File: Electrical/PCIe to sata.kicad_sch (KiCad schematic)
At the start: 106 parts, among them J10 87427-0442, J13 SATA-A-PL-SMT-K, J14 SATA-A-PL-SMT-K, J19 SATA-A-PL-SMT-K, J20 SATA-A-PL-SMT-K, J21 SATA-A-PL-SMT-K, J22 SATA-A-PL-SMT-K, J7 87427-0442, J8 87427-0442, J9 87427-0442, U11 W25Q128JVSIQ, U8 ASM1166, Y2 25MHz

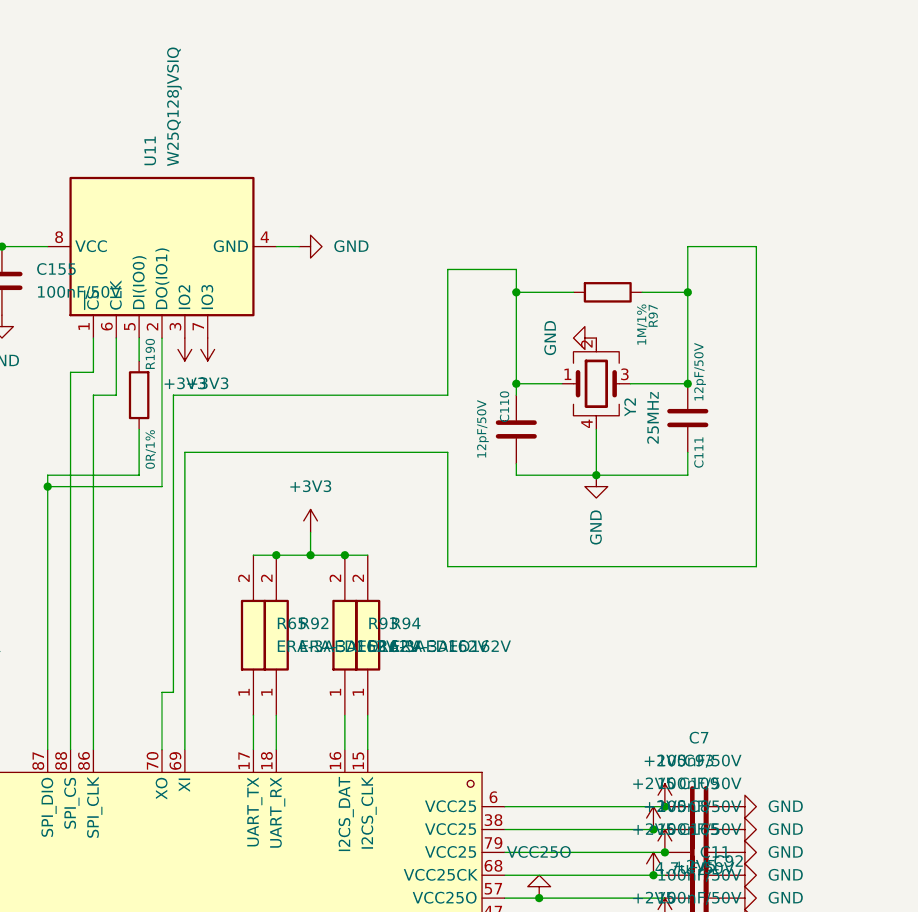
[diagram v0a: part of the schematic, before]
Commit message: add some fixes from initial prototype and fix 1v0 regulator
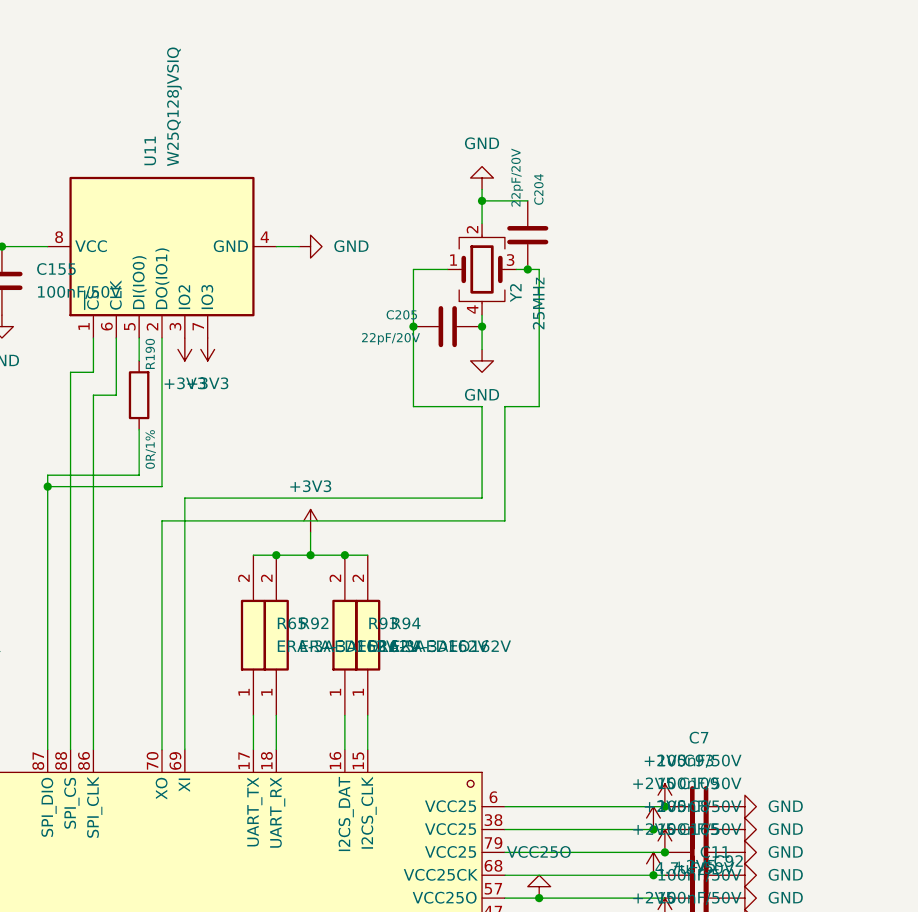
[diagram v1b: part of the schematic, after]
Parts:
- removed C110, C111: 12pF/50V, Capacitor_SMD:C_0402_1005Metric, symbol Device:C
- removed R97: 1M/1%, Resistor_SMD:R_0402_1005Metric, symbol Device:R
- added C204, C205: 22pF/20V, Capacitor_SMD:C_0402_1005Metric, symbol Device:C
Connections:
- net GND: now also C204.1, C205.2
- net at U8.69 (XI): now also Y2.1, C205.1; no longer Y2.3
- net at U8.70 (XO): now also Y2.3, C204.2; no longer Y2.1
